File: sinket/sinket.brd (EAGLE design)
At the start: 30 x 30 mm, 24 parts, among them IC1 ATTINY85-20PU, IC2 TS2940CP50S

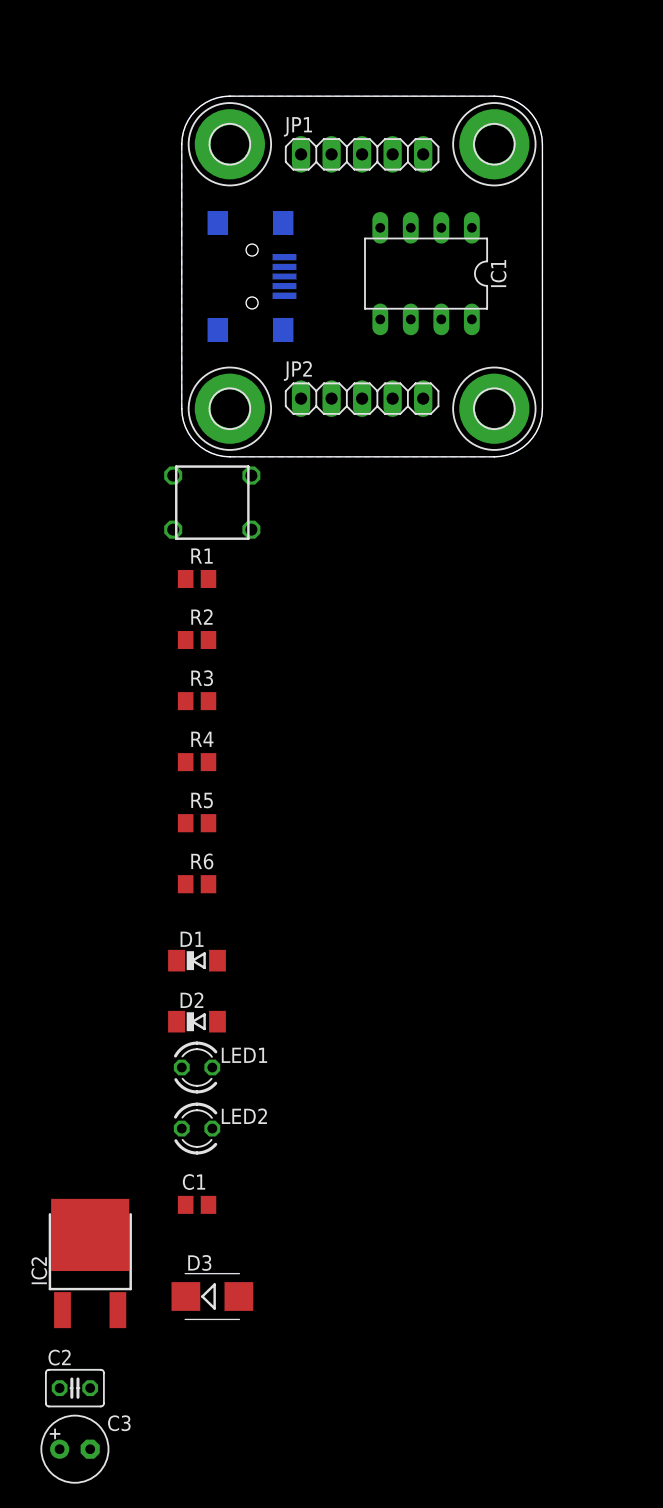
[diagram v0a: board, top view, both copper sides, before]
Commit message: changed board size to 36×36
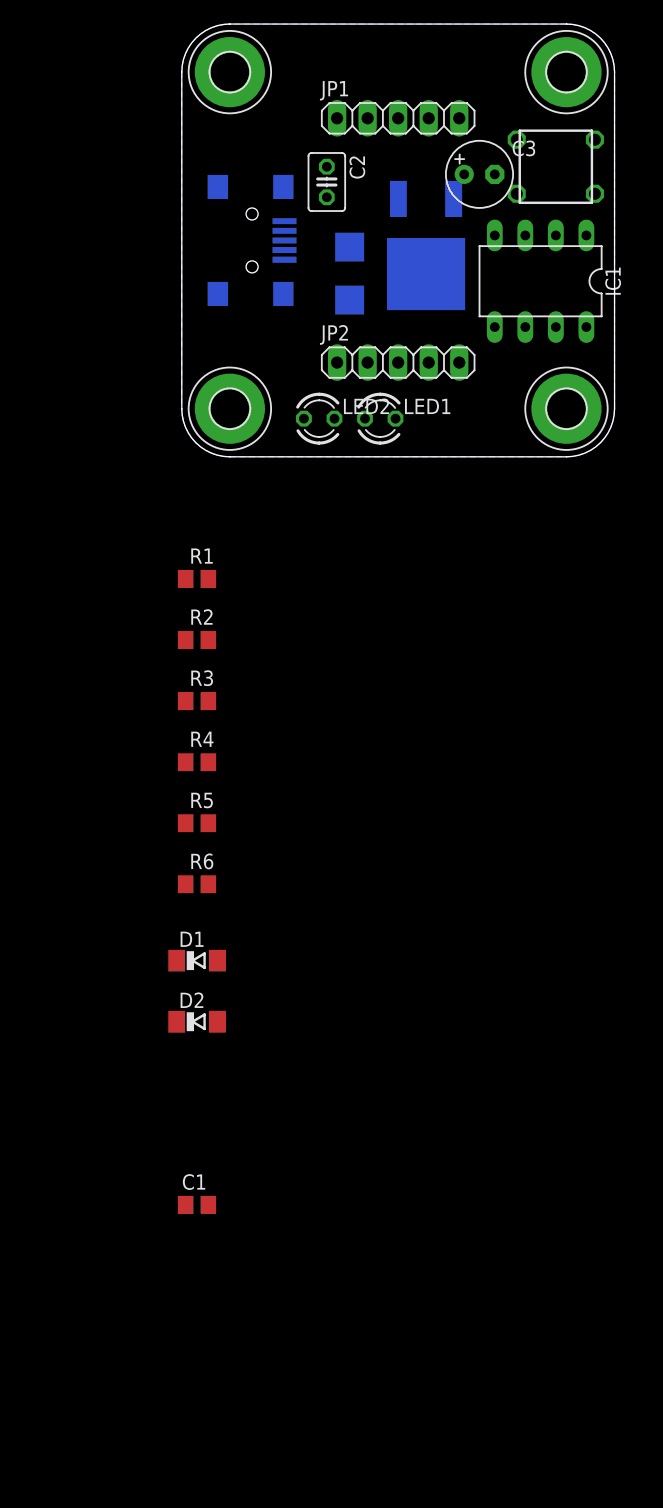
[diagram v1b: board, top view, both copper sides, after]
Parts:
- moved C3 111.3 mm to (24.8, 23.5)
- moved C2 102.5 mm to (12.1, 22.9), turned to 270 degrees
- moved IC2 92.0 mm to (20.3, 19.1), flipped to the bottom, turned to 180 degrees
- moved D3 85.9 mm to (14.0, 15.2), flipped to the bottom, turned to 270 degrees
- moved LED2 59.9 mm to (11.4, 3.17)
- moved LED1 56.1 mm to (16.5, 3.17)
- moved U$6 40.0 mm to (31.1, 24.1)
- moved IC1 9.55 mm to (29.8, 14.6)
- moved U$4 8.49 mm to (32.0, 32.0)
- moved U$3 6.00 mm to (32.0, 4.00)
- moved U$5 6.00 mm to (4.00, 32.0)
- moved JP1 4.24 mm to (18.0, 28.2)
- moved JP2 4.24 mm to (18.0, 7.84)
- moved U$1 3.00 mm to (5.85, 18.0)
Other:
- board size 30 x 30 mm -> 36 x 36 mm

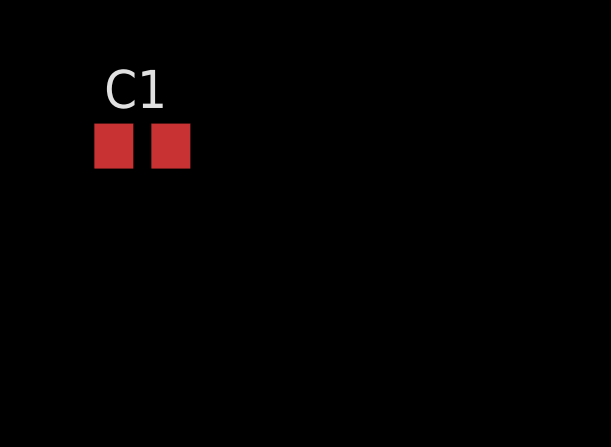
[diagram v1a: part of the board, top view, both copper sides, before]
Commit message: sinket: add fuse
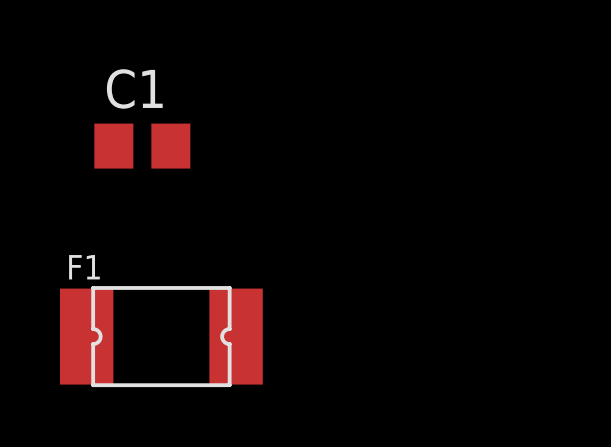
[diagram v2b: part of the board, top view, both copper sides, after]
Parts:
- added F1: SIBA_194600, n39:PTC-FUSE-1812
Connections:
- new net N$2: D3.A, F1.P$2
- net VBUS: now also F1.P$1; no longer D3.A
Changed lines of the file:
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@@
 <element name="C2" library="rcl" package="C025-030X050" value="470n" x="12.065" y="22.86" rot="R270"/>
 <element name="C3" library="rcl" package="E2,5-6" value="47u" x="24.765" y="23.495"/>
+<element name="F1" library="n39" package="PTC-FUSE-1812" value="SIBA_194600" x="1.905" y="-68.58"/>
 </elements>
 <signals>
@@
 <contactref element="U$1" pad="1"/>
 <contactref element="JP2" pad="1"/>
-<contactref element="D3" pad="A"/>
-<wire x1="12.92" y1="7.84" x2="13.97" y2="13.04" width="0" layer="19" extent="1-1"/>
+<contactref element="F1" pad="P$1"/>
+<wire x1="12.92" y1="7.84" x2="-0.585" y2="-68.58" width="0" layer="19" extent="1-1"/>
 <wire x1="8.55" y1="16.4" x2="12.92" y2="7.84" width="0" layer="19" extent="16-16"/>
 </signal>
@@
 <wire x1="20.54" y1="7.84" x2="31.115" y2="10.795" width="0" layer="19" extent="1-1"/>
 </signal>
+<signal name="N$2" class="1">
+<contactref element="F1" pad="P$2"/>
+<contactref element="D3" pad="A"/>
+<wire x1="13.97" y1="13.04" x2="4.395" y2="-68.58" width="0" layer="19" extent="1-16"/>
+</signal>
 </signals>

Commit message: start placing parts
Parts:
- moved C1 82.0 mm to (29.8, 14.6), flipped to the bottom
- moved F1 78.8 mm to (4.45, 10.2), flipped to the bottom, turned to 180 degrees
- moved D2 68.8 mm to (12.1, 21.0), flipped to the bottom, turned to 90 degrees
- moved D1 58.2 mm to (12.1, 15.2), flipped to the bottom, turned to 270 degrees
- moved R6 51.8 mm to (16.5, 14.0), flipped to the bottom
- moved R4 47.6 mm to (18.4, 19.1), flipped to the bottom
- moved R5 43.0 mm to (23.5, 6.35), flipped to the bottom, turned to 270 degrees
- moved R1 40.8 mm to (33.7, 14.6), flipped to the bottom, turned to 270 degrees
- moved R3 40.6 mm to (18.4, 16.5), flipped to the bottom
- moved R2 27.6 mm to (18.4, 6.35), flipped to the bottom, turned to 180 degrees
- moved C3 15.1 mm to (12.1, 31.8), turned to 270 degrees
- moved LED2 13.3 mm to (24.8, 3.17)
- moved IC2 12.7 mm to (19.7, 31.8), turned to 90 degrees
- moved D3 9.09 mm to (12.1, 6.35), turned to 0 degrees
- moved C2 5.46 mm to (7.62, 26.0), turned to 180 degrees
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
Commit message: change fuse package
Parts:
- D3: value MBRS240LT3 -> 1N5817-B; device diode:SMB -> diode:DO41-7.6
- F1: value SIBA_194600 -> (none); device n39:PTC-FUSE-1812 -> n39:LP60-050
- moved D3 2.25 mm to (10.5, 7.94), turned to 270 degrees
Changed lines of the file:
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@@
 <setting verticaltext="up"/>
 </settings>
-<grid distance="25" unitdist="mil" unit="mil" style="dots" multiple="1" display="yes" altdistance="25" altunitdist="mil" altunit="mil"/>
+<grid distance="12.5" unitdist="mil" unit="mil" style="dots" multiple="1" display="yes" altdistance="25" altunitdist="mil" altunit="mil"/>
 <layers>
 <layer number="1" name="Top" color="4" fill="1" visible="yes" active="yes"/>
@@
 <element name="LED2" library="led" package="LED3MM" value="green" x="24.765" y="3.175"/>
 <element name="C1" library="rcl" package="C0805" value="100n" x="29.845" y="14.605" rot="MR0"/>
-<element name="D3" library="diode" package="SMB" value="MBRS240LT3" x="12.065" y="6.35" rot="MR0"/>
+<element name="D3" library="diode" package="DO41-7.6" value="1N5817-B" x="10.4775" y="7.9375" rot="MR270"/>
 <element name="IC2" library="n39" package="TO-252" value="TS2940CP50S" x="19.685" y="31.75" rot="MR90">
 <attribute name="REICHELT" value="TS 2940 CP50" x="19.685" y="31.75" size="1.778" layer="28" rot="MR90" display="off"/>
@@
 <element name="C2" library="rcl" package="C025-030X050" value="470n" x="7.62" y="26.035" rot="R180"/>
 <element name="C3" library="rcl" package="E2,5-6" value="47u" x="12.065" y="31.75" rot="R270"/>
-<element name="F1" library="n39" package="PTC-FUSE-1812" value="SIBA_194600" x="4.445" y="10.16" rot="MR180"/>
+<element name="F1" library="n39" package="LP60-050" value="" x="4.445" y="10.16" rot="MR180"/>
 </elements>
 <signals>
@@
 <wire x1="23.08" y1="10.38" x2="17.46" y2="13.97" width="0" layer="19" extent="16-16"/>
 <wire x1="23.495" y1="7.3" x2="23.08" y2="10.38" width="0" layer="19" extent="16-16"/>
-<wire x1="14.265" y1="6.35" x2="17.46" y2="13.97" width="0" layer="19" extent="16-16"/>
+<wire x1="10.4775" y1="11.7475" x2="17.46" y2="13.97" width="0" layer="19" extent="16-16"/>
 <wire x1="30.795" y1="14.605" x2="23.08" y2="10.38" width="0" layer="19" extent="16-16"/>
 <wire x1="33.655" y1="13.655" x2="30.795" y2="14.605" width="0" layer="19" extent="16-16"/>
@@
 <contactref element="F1" pad="P$1"/>
 <wire x1="12.92" y1="10.38" x2="8.55" y2="16.4" width="0" layer="19" extent="16-16"/>
-<wire x1="1.955" y1="10.16" x2="8.55" y2="16.4" width="0" layer="19" extent="16-16"/>
+<wire x1="2.395" y1="9.61" x2="8.55" y2="16.4" width="0" layer="19" extent="16-16"/>
 </signal>
 <signal name="GND" class="1">
@@
 <contactref element="F1" pad="P$2"/>
 <contactref element="D3" pad="A"/>
-<wire x1="9.865" y1="6.35" x2="6.935" y2="10.16" width="0" layer="19" extent="16-16"/>
+<wire x1="10.4775" y1="4.1275" x2="6.495" y2="10.71" width="0" layer="19" extent="16-16"/>
 </signal>
 </signals>

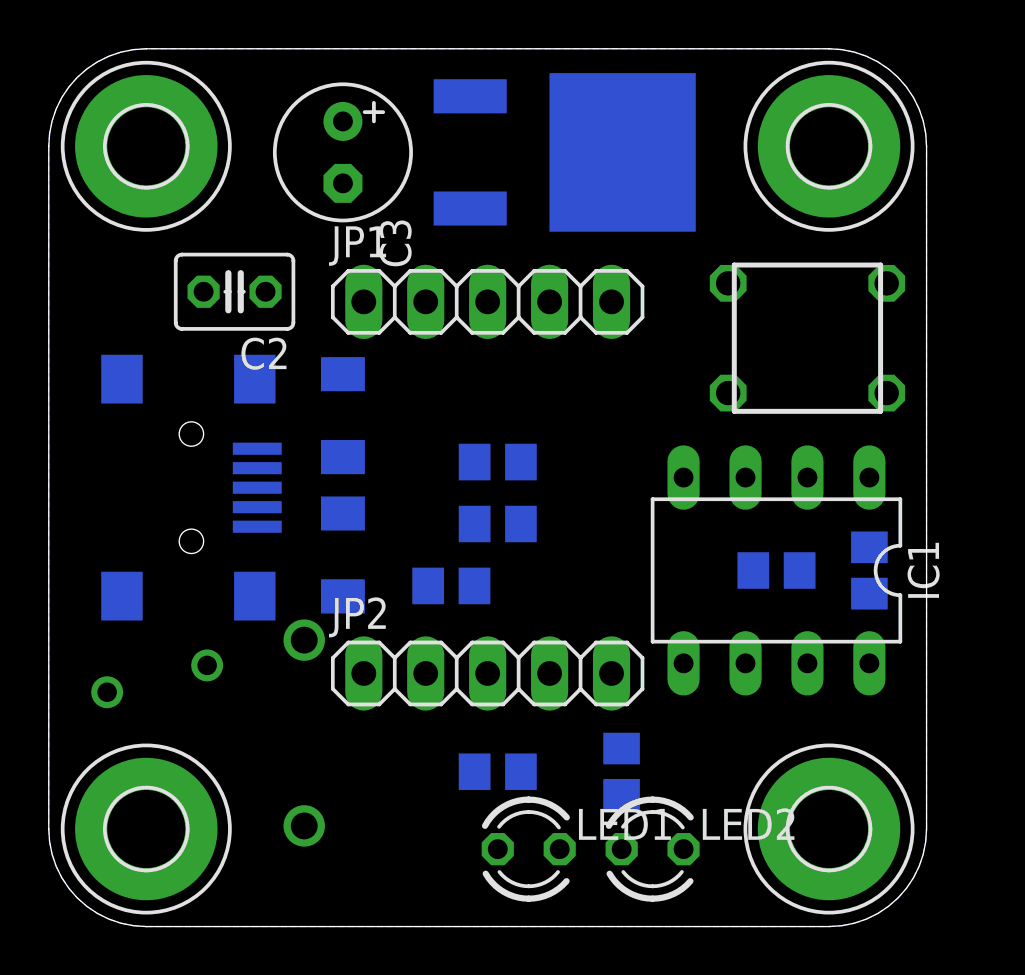
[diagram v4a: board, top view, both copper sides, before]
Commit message: replace all 0805 parts with 1206 and start routing
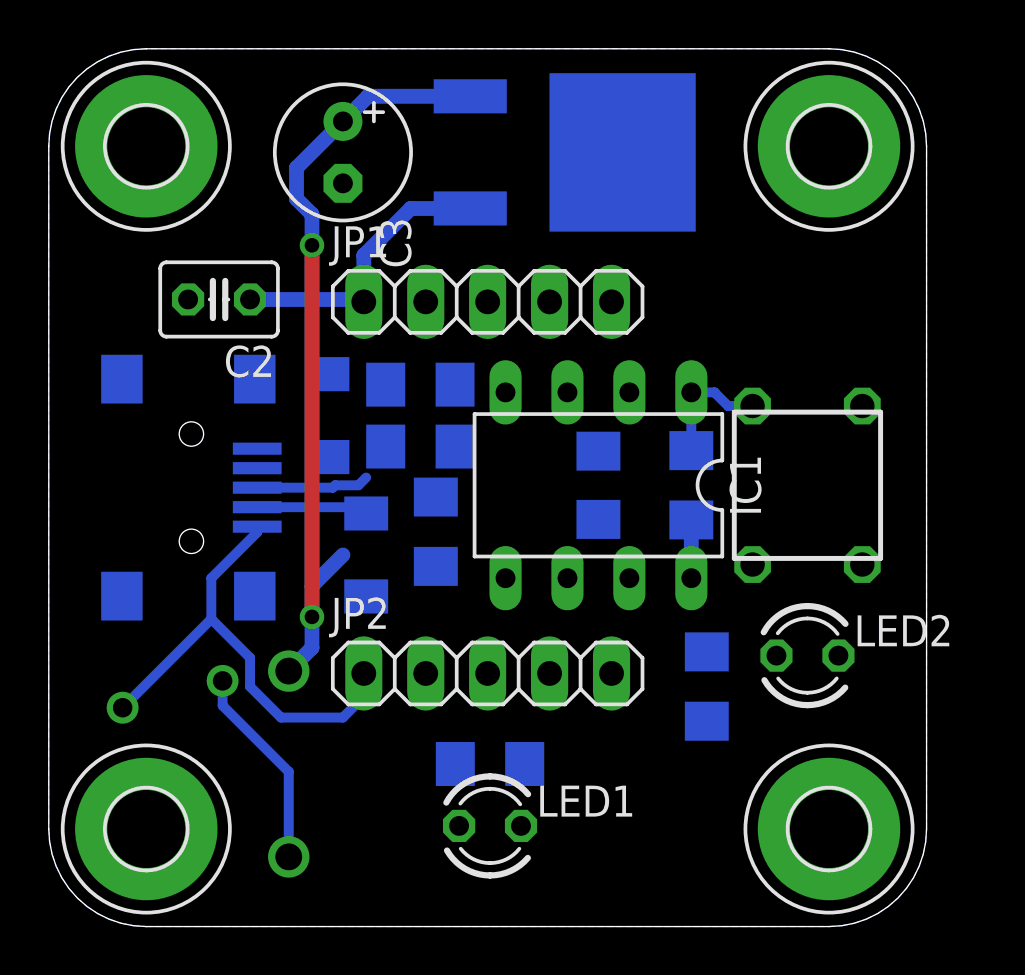
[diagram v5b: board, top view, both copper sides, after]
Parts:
- C1: device rcl:C0805 -> rcl:C1206
- R1, R2, R3, R4, R5, R6: device rcl:R0805 -> rcl:R1206
- moved LED2 10.2 mm to (31.1, 11.1)
- moved R1 8.09 mm to (26.4, 18.1)
- moved C1 8.09 mm to (22.5, 18.1), turned to 90 degrees
- moved IC1 8.09 mm to (22.5, 18.1)
- moved U$6 6.03 mm to (31.1, 18.1), turned to 90 degrees
- moved R5 4.94 mm to (27.0, 9.84), turned to 90 degrees
- moved R4 4.49 mm to (15.2, 22.2)
- moved R3 4.49 mm to (15.2, 19.7)
- moved R6 2.31 mm to (15.9, 16.2), turned to 90 degrees
- moved LED1 1.85 mm to (18.1, 4.13)
- moved D3 1.42 mm to (9.84, 6.67)
- moved D1 0.95 mm to (13.0, 15.2)
- moved F1 0.90 mm to (5.08, 9.53)
- moved C2 0.71 mm to (6.99, 25.7)
- moved D2 0.63 mm to (11.4, 21.0), turned to 270 degrees
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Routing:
- net +5V: track 0.00 -> 35.6 mm, vias 0 -> 2
- net VBUS: track 0.00 -> 19.6 mm
- net VBAT: track 0.00 -> 11.8 mm
- net N$2: track 0.00 -> 8.34 mm
- net !RESET: track 0.00 -> 5.13 mm
- net N$3: track 0.00 -> 4.64 mm
- net N$1: track 0.00 -> 4.58 mm

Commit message: finish routing
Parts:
- moved R3 1.14 mm to (15.9, 18.7)
- moved R6 0.95 mm to (15.9, 15.2)
- moved D1 0.32 mm to (13.0, 14.9)
- turned LED1 to 180 degrees
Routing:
- net +5V: track 35.6 -> 60.6 mm
- net B3: track 0.00 -> 16.7 mm
- net !RESET: track 5.13 -> 16.8 mm
- net B1: track 0.00 -> 10.1 mm
- net B4: track 0.00 -> 8.95 mm
- net N$3: track 4.64 -> 11.3 mm
- net B2: track 0.00 -> 5.82 mm
- net B0: track 0.00 -> 5.82 mm
- net N$1: track 4.58 -> 9.87 mm
- net N$5: track 0.00 -> 2.92 mm
- net N$4: track 0.00 -> 2.69 mm

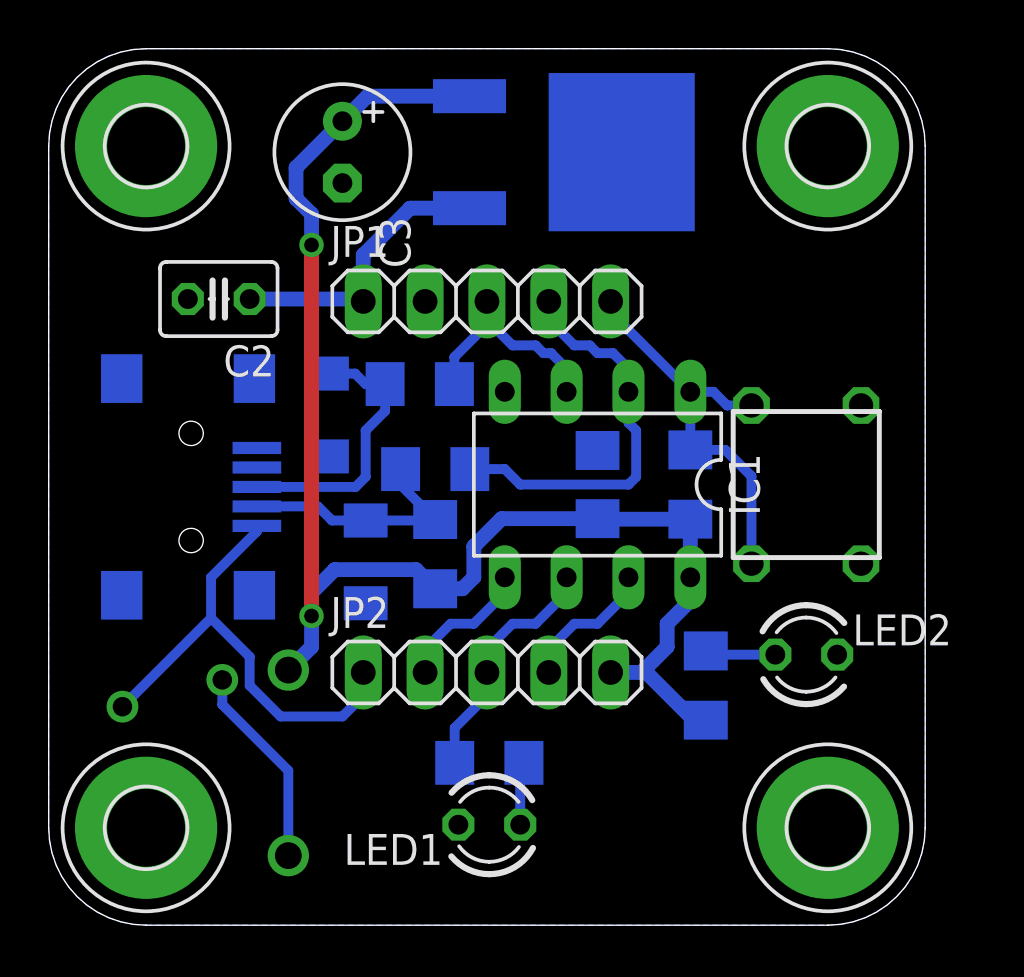
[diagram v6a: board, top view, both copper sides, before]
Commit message: did DRC, added text and space for logo
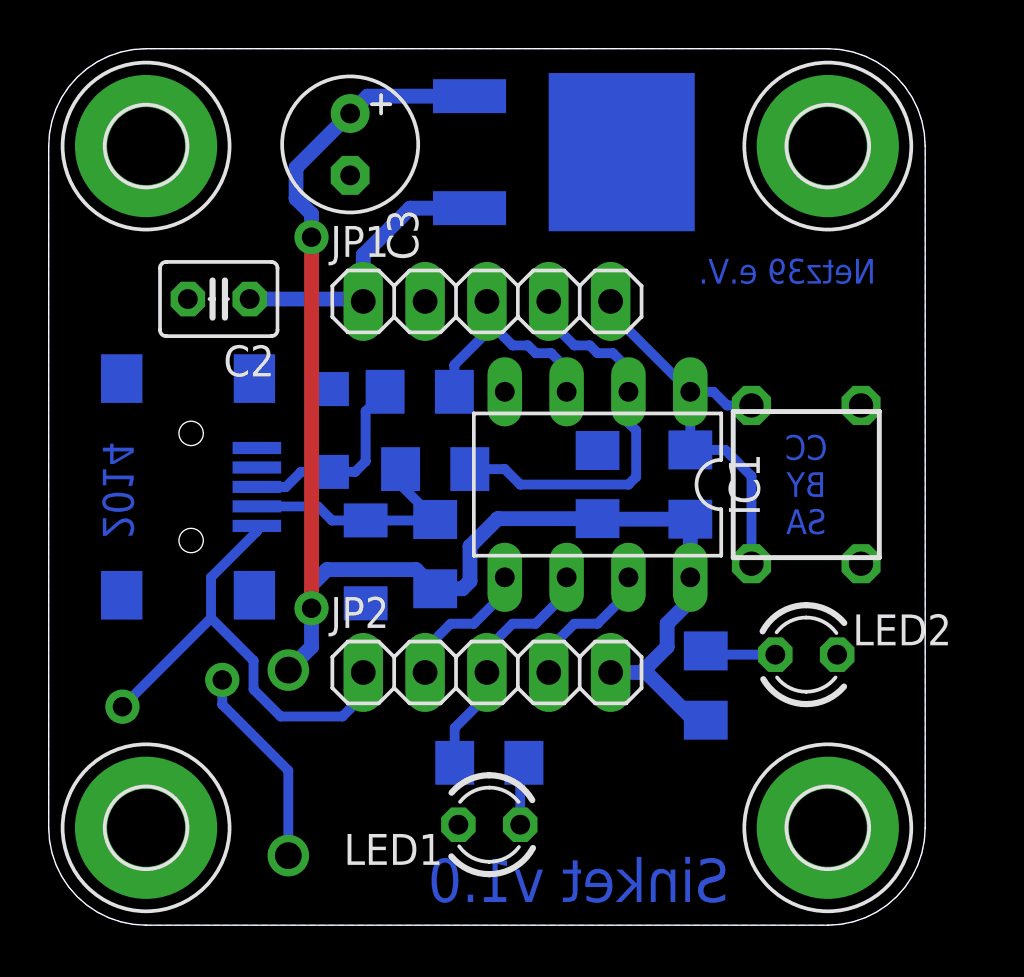
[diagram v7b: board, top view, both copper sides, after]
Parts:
- moved D2 0.63 mm to (11.4, 20.3), turned to 90 degrees
- moved C3 0.45 mm to (12.4, 32.1)
- moved R4 0.32 mm to (15.2, 21.9)
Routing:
- net N$3: track 11.3 -> 8.09 mm
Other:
- board text added: "2014"
- board text added: "CC BY SA"
- board text added: "Netz39 e.V."
- board text added: "Sinket v1.0"
